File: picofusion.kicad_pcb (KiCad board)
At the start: 2 copper layers, 1 part

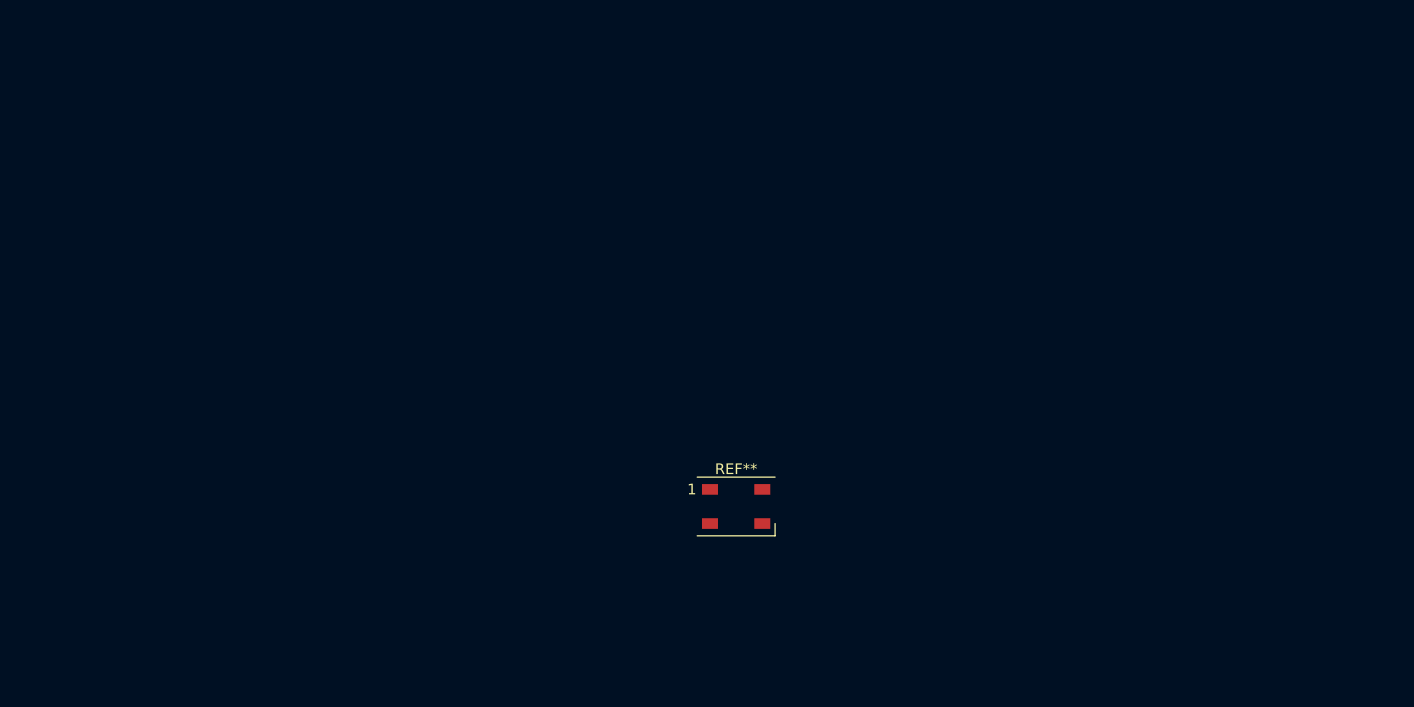
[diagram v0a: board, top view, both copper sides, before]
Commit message: finish schematic draft
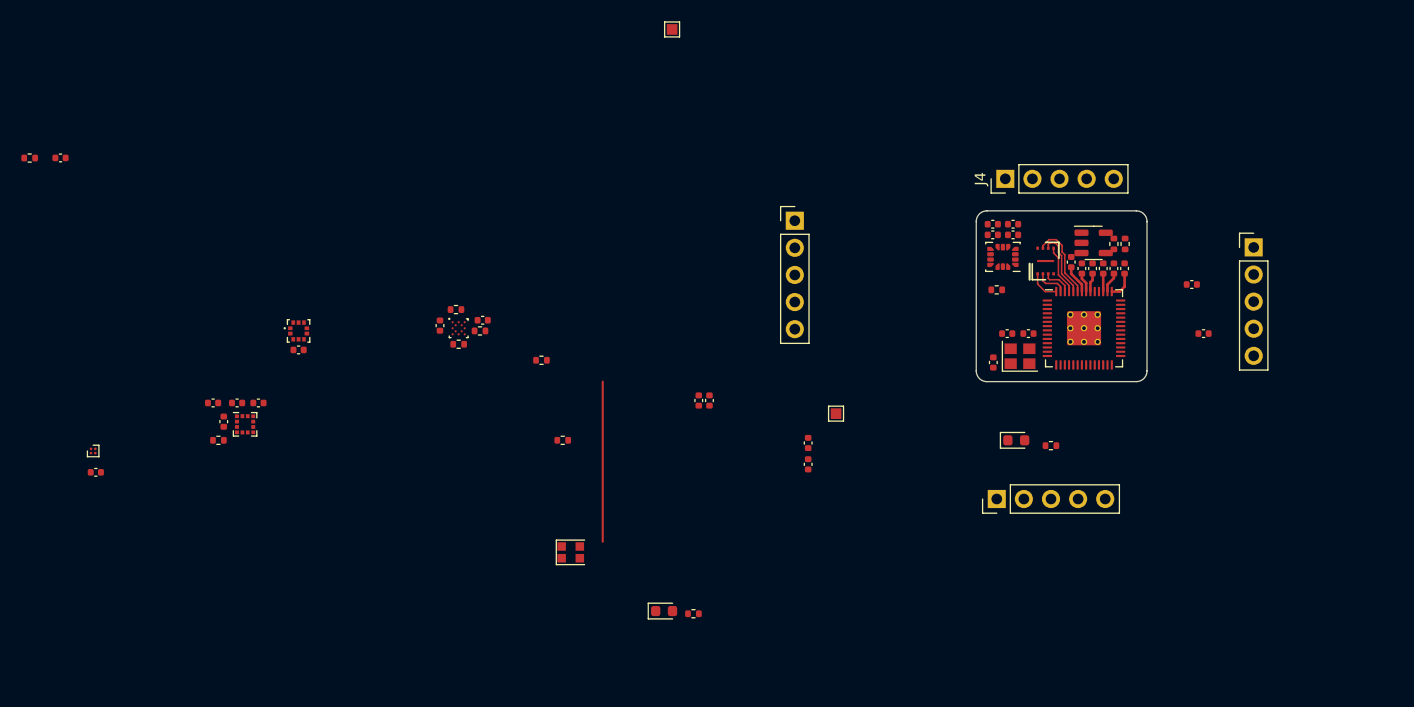
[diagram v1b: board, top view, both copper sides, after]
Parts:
- removed REF**: LED_WS2812B_PLCC4_5.0x5.0mm_P3.2mm, LED_SMD:LED_WS2812B_PLCC4_5.0x5.0mm_P3.2mm
- added C1: 0.1uF, Capacitor_SMD:C_0402_1005Metric, F.Cu at (154.9, 38.8)
- added C10: 0.1uF, Capacitor_SMD:C_0402_1005Metric, F.Cu at (155.9, 39.4)
- added C11: 0.1uF, Capacitor_SMD:C_0402_1005Metric, F.Cu at (60.2, 29.0)
- added C12: 0.1uF, Capacitor_SMD:C_0402_1005Metric, F.Cu at (156.9, 39.4)
- added C13: 0.1uF, Capacitor_SMD:C_0402_1005Metric, F.Cu at (159.9, 39.4)
- added C14: 0.1uF, Capacitor_SMD:C_0402_1005Metric, F.Cu at (166.2, 40.9)
- added C15: 1uF, Capacitor_SMD:C_0402_1005Metric, F.Cu at (158.9, 39.4)
- added C16: 1uF, Capacitor_SMD:C_0402_1005Metric, F.Cu at (130.2, 55.8)
- added C17: 1uF, Capacitor_SMD:C_0402_1005Metric, F.Cu at (130.2, 57.8)
- added C19: 2.2uF, Capacitor_SMD:C_0402_1005Metric, F.Cu at (147.6, 36.2)
- added C2: 0.1uF, Capacitor_SMD:C_0402_1005Metric, F.Cu at (121.0, 51.8)
- added C20: 0.1uF, Capacitor_SMD:C_0402_1005Metric, F.Cu at (147.6, 35.2)
- added C21: 0.1uF, Capacitor_SMD:C_0402_1005Metric, F.Cu at (99.8, 44.2)
- added C22: 0.1uF, Capacitor_SMD:C_0402_1005Metric, F.Cu at (95.8, 44.8)
- added C23: 10nF, Capacitor_SMD:C_0402_1005Metric, F.Cu at (149.4, 36.2)
- added C24: 10uF, Capacitor_SMD:C_0402_1005Metric, F.Cu at (75.5, 53.8)
- added C25: 0.1uF, Capacitor_SMD:C_0402_1005Metric, F.Cu at (74.5, 52.0)
- added C26: 0.1uF, Capacitor_SMD:C_0402_1005Metric, F.Cu at (78.7, 52.0)
- added C27: 220nF, Capacitor_SMD:C_0402_1005Metric, F.Cu at (76.7, 52.0)
- added C28: 0.1uF, Capacitor_SMD:C_0402_1005Metric, F.Cu at (82.5, 47.0)
- added C29: 2.2uF, Capacitor_SMD:C_0402_1005Metric, F.Cu at (63.5, 58.5)
- added C3: 1uF, Capacitor_SMD:C_0402_1005Metric, F.Cu at (157.9, 39.4)
- added C4: 0.1uF, Capacitor_SMD:C_0402_1005Metric, F.Cu at (149.4, 35.2)
- added C5: 12pF, Capacitor_SMD:C_0402_1005Metric, F.Cu at (147.6, 48.2)
- added C6: 0.1uF, Capacitor_SMD:C_0402_1005Metric, F.Cu at (150.9, 45.5)
- added C7: 0.1uF, Capacitor_SMD:C_0402_1005Metric, F.Cu at (167.3, 45.5)
- added C8: 12pF, Capacitor_SMD:C_0402_1005Metric, F.Cu at (148.9, 45.5)
- added C9: 0.1uF, Capacitor_SMD:C_0402_1005Metric, F.Cu at (120.0, 51.8)
- added D1: WS2812B-2020, LED_SMD_Extra:WS2812B-2020, F.Cu at (108.0, 66.0)
- added D2: RED, LED_SMD:LED_0603_1608Metric, F.Cu at (116.8, 71.5)
- added D3: LED, LED_SMD:LED_0603_1608Metric, F.Cu at (149.8, 55.5)
- added J1: EAST, Connector_PinHeader_2.54mm:PinHeader_1x05_P2.54mm_Vertical, F.Cu at (129.0, 34.9)
- added J2: WEST, Connector_PinHeader_2.54mm:PinHeader_1x05_P2.54mm_Vertical, F.Cu at (147.9, 61.0)
- added J3: SOUTH, Connector_PinHeader_2.54mm:PinHeader_1x05_P2.54mm_Vertical, F.Cu at (172.0, 37.4)
- added J4: NORTH, Connector_PinHeader_2.54mm:PinHeader_1x05_P2.54mm_Vertical, F.Cu at (148.7, 31.0)
- added R1: 10K, Resistor_SMD:R_0402_1005Metric, F.Cu at (57.3, 29.1)
- added R13: 10K, Resistor_SMD:R_0402_1005Metric, F.Cu at (147.9, 41.4)
- added R14: 10K, Resistor_SMD:R_0402_1005Metric, F.Cu at (97.2, 43.2)
- added R15: 10K, Resistor_SMD:R_0402_1005Metric, F.Cu at (97.5, 46.5)
- added R16: 10K, Resistor_SMD:R_0402_1005Metric, F.Cu at (99.5, 45.2)
- added R17: 10K, Resistor_SMD:R_0402_1005Metric, F.Cu at (75.0, 55.5)
- added R18: 1K, Resistor_SMD:R_0402_1005Metric, F.Cu at (153.0, 56.0)
- added R2: 27.4, Resistor_SMD:R_0402_1005Metric, F.Cu at (158.9, 37.1)
- added R3: 27.4, Resistor_SMD:R_0402_1005Metric, F.Cu at (159.9, 37.1)
- added R4: 10K, Resistor_SMD:R_0402_1005Metric, F.Cu at (105.3, 48.0)
- added R5: 10K, Resistor_SMD:R_0402_1005Metric, F.Cu at (107.2, 55.5)
- added R6: 1K, Resistor_SMD:R_0402_1005Metric, F.Cu at (119.5, 71.8)
- added TP1: QSPI_SCK, TestPoint:TestPoint_Pad_1.0x1.0mm, F.Cu at (117.5, 17.0)
- added TP2: TestPoint, TestPoint:TestPoint_Pad_1.0x1.0mm, F.Cu at (132.9, 53.0)
- added U1: W25Q16, USON:8-USON, F.Cu at (152.5, 38.7)
- added U2: RP2040, RP2040_minimal:RP2040-QFN-56, F.Cu at (156.1, 45.0)
- added U3: BL9161-33BARN, Package_TO_SOT_SMD:SOT-23-5, F.Cu at (157.0, 37.0)
- added U4: ICM42605, Package_LGA:LGA-14_3x2.5mm_P0.5mm_LayoutBorder3x4y, F.Cu at (148.5, 38.3)
- added U5: BMM150, Package_CSP:WLCSP-12_1.56x1.56mm_P0.4mm, F.Cu at (97.5, 45.0)
- added U6: LIS2MDLTR, Package_LGA:LGA-12_2x2mm_P0.5mm, F.Cu at (77.5, 54.0)
- added U7: ICP-10100, ICP-10100:PQFN50P200X200X80-10N, F.Cu at (82.5, 45.2)
- added U8: MMC5633NJL, Package_BGA:WLP-4_0.86x0.86mm_P0.4mm, F.Cu at (63.2, 56.5)
- added Y1: 12MHz, Crystal:Crystal_SMD_2520-4Pin_2.5x2.0mm, F.Cu at (150.1, 47.6)
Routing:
- net +3V3: track 0.00 -> 8.16 mm
- net /QSPI_SD3: track 0.00 -> 7.41 mm
- net /QSPI_SCLK: track 0.00 -> 6.33 mm
- net /QSPI_SD0: track 0.00 -> 4.66 mm
- net +1V1: track 0.00 -> 4.38 mm
- net /QSPI_SS: track 0.00 -> 3.00 mm
- net /QSPI_SD1: track 0.00 -> 2.99 mm
- net /QSPI_SD2: track 0.00 -> 2.82 mm
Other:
- board outline added: 16 x 16 mm
- copper layers 2 -> 4

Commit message: schematic: update regulator, sensors
* simplify some sensor schematics
* replace 3v3 regulator
* DRC and footprints
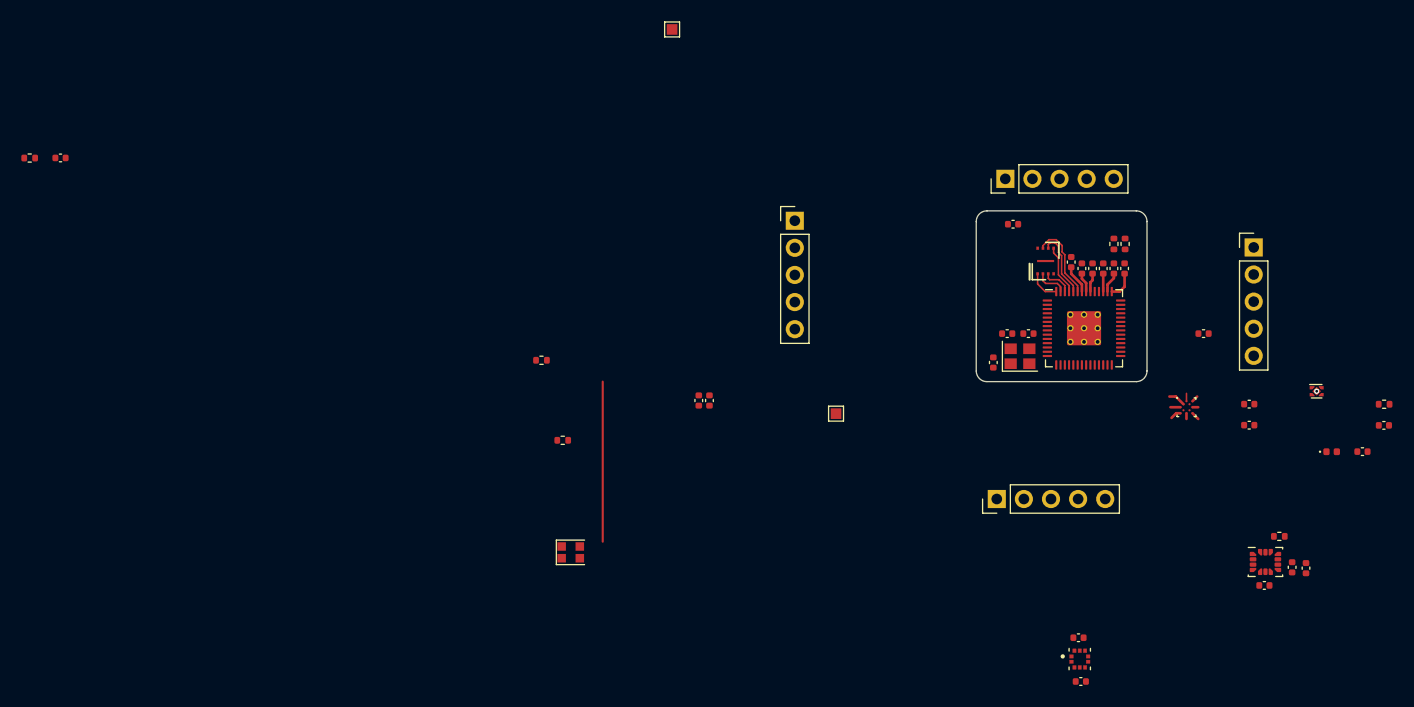
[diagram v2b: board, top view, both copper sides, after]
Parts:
- removed C24: 10uF, Capacitor_SMD:C_0402_1005Metric
- removed C25, C26, C28: 0.1uF, Capacitor_SMD:C_0402_1005Metric
- removed C27: 220nF, Capacitor_SMD:C_0402_1005Metric
- removed C29: 2.2uF, Capacitor_SMD:C_0402_1005Metric
- removed D3: LED, LED_SMD:LED_0603_1608Metric
- removed R13, R14, R15, R16, R17: 10K, Resistor_SMD:R_0402_1005Metric
- removed R18: 1K, Resistor_SMD:R_0402_1005Metric
- removed U7: ICP-10100, ICP-10100:PQFN50P200X200X80-10N
- removed U8: MMC5633NJL, Package_BGA:WLP-4_0.86x0.86mm_P0.4mm
- added C18: 0.1uF, Capacitor_SMD:C_0402_1005Metric, F.Cu at (175.6, 67.4)
- added R7: 10K, Resistor_SMD:R_0402_1005Metric, F.Cu at (174.4, 64.5)
- C16: value 1uF -> 0.1uF
- C17: value 1uF -> 2.2uF
- C19: value 2.2uF -> 10nF
- C23: value 10nF -> 0.1uF
- D2: footprint LED_SMD:LED_0603_1608Metric -> LED_SMD:LED_0402_1005Metric
- R6: value 1K -> 470
- U3: value BL9161-33BARN -> TLV71333PDQNT; footprint Package_TO_SOT_SMD:SOT-23-5 -> Package_SON:Texas_X2SON-4_1x1mm_P0.65mm
- U6: value LIS2MDLTR -> ICP20100; footprint Package_LGA:LGA-12_2x2mm_P0.5mm -> ICP20100:PQFN50P200X200X85-10N
- moved U6 81.2 mm to (155.7, 76.0)
- moved C21 72.5 mm to (171.6, 54.1)
- moved C22 68.7 mm to (155.8, 78.1), turned to 0 degrees
- moved U5 68.6 mm to (165.7, 52.4)
- moved R6 67.6 mm to (184.2, 52.1)
- moved D2 64.3 mm to (179.3, 56.6)
- moved C16 51.9 mm to (182.2, 56.6), turned to 0 degrees
- moved C17 47.7 mm to (176.9, 67.5)
- moved C19 41.6 mm to (173.0, 69.1), turned to 0 degrees
- moved C23 38.2 mm to (155.6, 74.0)
- moved U4 37.7 mm to (173.1, 66.9), turned to 0 degrees
- moved C20 29.4 mm to (171.6, 52.1), turned to 0 degrees
- moved U3 25.1 mm to (177.9, 50.9)
- moved C14 22.3 mm to (184.2, 54.1)
- renumbered TP2 to 3V3
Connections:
- C14 pad 1: +3V3 -> +5V
- C16 pad 1: +5V -> +3V3
- C17 pad 1: +3V3 -> GND
- C17 pad 2: GND -> +3V3
- C19 pad 1: GND -> +3V3
- C19 pad 2: +3V3 -> GND
- C22 pad 1: +3V3 -> GND
- C22 pad 2: GND -> +3V3
- U2 pad 2: /SPI0_MISO -> /SPI0_POCI
- U2 pad 5: /SPI0_MOSI -> /SPI0_POCI
- U2 pad 8: /DRDY_LIS2MDL -> /SPI0_nCS
- U2 pad 9: /DRDY_BMM150 -> unconnected-(U2-Pad9)
- U3 pad 4: (no net) -> unconnected-(U3-Pad4)
- U4 pad 12: Net-(R13-Pad2) -> /SPI0_nCS
- U4 pad 9: unconnected-(U4-Pad9) -> GND
- U5 pad A1: Net-(R16-Pad1) -> +3V3
- U5 pad A5: Net-(R15-Pad1) -> GND
- U5 pad C1: Net-(R14-Pad1) -> GND
- U5 pad D4: /DRDY_BMM150 -> unconnected-(U5-PadD4)
- U6 pad 1: /I2C0_SCL -> +3V3
- U6 pad 2: (no net) -> /I2C0_SCL
- U6 pad 3: Net-(R17-Pad1) -> GND
- U6 pad 5: Net-(C27-Pad1) -> +3V3
- U6 pad 7: /DRDY_LIS2MDL -> unconnected-(U6-Pad7)
- U6 pad 9: +3V3 -> GND
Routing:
- net GND: track 0.00 -> 3.63 mm
- net +3V3: track 8.16 -> 10.5 mm, vias 0 -> 1
- net /I2C0_SCL: track 0.00 -> 0.73 mm

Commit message: draft layout improvements
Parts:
- moved C17 50.1 mm to (139.6, 34.0), turned to -90 degrees
- moved U4 48.0 mm to (137.3, 34.9)
- moved C18 47.8 mm to (139.6, 35.9), turned to 90 degrees
- moved C19 47.4 mm to (138.1, 37.0)
- moved R7 47.1 mm to (136.1, 37.0)
- moved C14 44.3 mm to (142.1, 40.4), turned to -90 degrees
- moved D1 42.7 mm to (148.2, 51.5)
- moved C16 42.4 mm to (143.6, 39.1)
- moved U3 35.9 mm to (143.6, 40.4)
- moved C7 16.8 mm to (150.8, 42.4), turned to 180 degrees
- moved R3 2.15 mm to (157.8, 37.0)
- moved R2 2.10 mm to (156.8, 37.0)
- moved C4 1.95 mm to (149.4, 37.2)
- moved C1 0.40 mm to (154.9, 39.2)
- moved C12 0.40 mm to (156.9, 39.8)
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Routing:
- net /XOUT: track 0.00 -> 2.18 mm
- net /XIN: track 0.00 -> 1.58 mm
- net +1V1: track 4.38 -> 3.58 mm

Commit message: backup before moving to 0201
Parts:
- moved C22 36.2 mm to (141.1, 45.0), turned to -90 degrees
- moved U6 35.3 mm to (139.3, 44.7)
- moved C23 35.2 mm to (139.0, 42.9)
- moved C17 12.0 mm to (150.6, 38.6)
- moved C18 12.0 mm to (150.6, 40.5)
- moved R7 11.9 mm to (147.2, 41.3)
- moved C19 11.9 mm to (149.2, 41.3)
- moved U4 11.9 mm to (148.3, 39.2)
- moved R2 0.49 mm to (156.8, 37.5)
- moved R3 0.49 mm to (157.8, 37.5)
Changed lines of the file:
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@@
   )
   (footprint "Capacitor_SMD:C_0402_1005Metric" (layer "F.Cu")
-    (at 139.6 34 -90)
+    (at 150.6375 38.65 -90)
     (descr "Capacitor SMD 0402 (1005 Metric), square (rectangular) end terminal, IPC_7351 nominal, (Body size source: IPC-SM-782 page 76, https://www.pcb-3d.com/wordpress/wp-content/uploads/ipc-sm-782a_amendment_1_and_2.pdf), generated with kicad-footprint-generator")
     (tags "capacitor")
@@
   )
   (footprint "Package_LGA:LGA-14_3x2.5mm_P0.5mm_LayoutBorder3x4y" (layer "F.Cu")
-    (at 137.3 34.92)
+    (at 148.3375 39.25)
     (descr "LGA, 14 Pin (http://www.st.com/resource/en/datasheet/lsm6ds3.pdf), generated with kicad-footprint-generator ipc_noLead_generator.py")
     (tags "LGA NoLead")
@@
   )
   (footprint "Capacitor_SMD:C_0402_1005Metric" (layer "F.Cu")
-    (at 139.6 35.9 90)
+    (at 150.6375 40.55 90)
     (descr "Capacitor SMD 0402 (1005 Metric), square (rectangular) end terminal, IPC_7351 nominal, (Body size source: IPC-SM-782 page 76, https://www.pcb-3d.com/wordpress/wp-content/uploads/ipc-sm-782a_amendment_1_and_2.pdf), generated with kicad-footprint-generator")
     (tags "capacitor")
@@
   )
   (footprint "Resistor_SMD:R_0402_1005Metric" (layer "F.Cu")
-    (at 156.8 37 90)
+    (at 156.8 37.49 90)
     (descr "Resistor SMD 0402 (1005 Metric), square (rectangular) end terminal, IPC_7351 nominal, (Body size source: IPC-SM-782 page 72, https://www.pcb-3d.com/wordpress/wp-content/uploads/ipc-sm-782a_amendment_1_and_2.pdf), generated with kicad-footprint-generator")
     (tags "resistor")
@@
   )
   (footprint "ICP20100:PQFN50P200X200X85-10N" (layer "F.Cu")
-    (at 155.7 76)
+    (at 139.3 44.7)
     (property "Sheetfile" "sensors.kicad_sch")
     (property "Sheetname" "Sensor Suite")
@@
   )
   (footprint "Resistor_SMD:R_0402_1005Metric" (layer "F.Cu")
-    (at 136.11 37)
+    (at 147.2375 41.33)
     (descr "Resistor SMD 0402 (1005 Metric), square (rectangular) end terminal, IPC_7351 nominal, (Body size source: IPC-SM-782 page 72, https://www.pcb-3d.com/wordpress/wp-content/uploads/ipc-sm-782a_amendment_1_and_2.pdf), generated with kicad-footprint-generator")
     (tags "resistor")
@@
   )
   (footprint "Capacitor_SMD:C_0402_1005Metric" (layer "F.Cu")
-    (at 138.12 37)
+    (at 149.1575 41.33)
     (descr "Capacitor SMD 0402 (1005 Metric), square (rectangular) end terminal, IPC_7351 nominal, (Body size source: IPC-SM-782 page 76, https://www.pcb-3d.com/wordpress/wp-content/uploads/ipc-sm-782a_amendment_1_and_2.pdf), generated with kicad-footprint-generator")
     (tags "capacitor")
@@
   )
   (footprint "Capacitor_SMD:C_0402_1005Metric" (layer "F.Cu")
-    (at 155.8 78.1)
+    (at 141.1 45 -90)
     (descr "Capacitor SMD 0402 (1005 Metric), square (rectangular) end terminal, IPC_7351 nominal, (Body size source: IPC-SM-782 page 76, https://www.pcb-3d.com/wordpress/wp-content/uploads/ipc-sm-782a_amendment_1_and_2.pdf), generated with kicad-footprint-generator")
     (tags "capacitor")
@@
     (property "Sheetname" "Sensor Suite")
     (attr smd)
-    (fp_text reference "C22" (at 0 -1.16) (layer "F.SilkS") hide
-      (effects (font (size 1 1) (thickness 0.15)))
-    )
-    (fp_text value "0.1uF" (at 0 1.16) (layer "F.Fab")
-      (effects (font (size 1 1) (thickness 0.15)))
-    )
-    (fp_text user "${REFERENCE}" (at 0 0) (layer "F.Fab")
-      (effects (font (size 0.25 0.25) (thickness 0.04)))
-    )
-    (fp_line (start -0.107836 -0.36) (end 0.107836 -0.36) (layer "F.SilkS") (width 0.12))
-    (fp_line (start -0.107836 0.36) (end 0.107836 0.36) (layer "F.SilkS") (width 0.12))
-    (fp_line (start 0.91 -0.46) (end 0.91 0.46) (layer "F.CrtYd") (width 0.05))
-    (fp_line (start 0.91 0.46) (end -0.91 0.46) (layer "F.CrtYd") (width 0.05))
-    (fp_line (start -0.91 0.46) (end -0.91 -0.46) (layer "F.CrtYd") (width 0.05))
-    (fp_line (start -0.91 -0.46) (end 0.91 -0.46) (layer "F.CrtYd") (width 0.05))
-    (fp_line (start 0.5 -0.25) (end 0.5 0.25) (layer "F.Fab") (width 0.1))
-    (fp_line (start 0.5 0.25) (end -0.5 0.25) (layer "F.Fab") (width 0.1))
-    (fp_line (start -0.5 -0.25) (end 0.5 -0.25) (layer "F.Fab") (width 0.1))
-    (fp_line (start -0.5 0.25) (end -0.5 -0.25) (layer "F.Fab") (width 0.1))
-    (pad "1" smd roundrect locked (at -0.48 0) (size 0.56 0.62) (layers "F.Cu" "F.Paste" "F.Mask") (roundrect_rratio 0.25)
-      (net 2 "GND") (pintype "passive"))
-    (pad "2" smd roundrect locked (at 0.48 0) (size 0.56 0.62) (layers "F.Cu" "F.Paste" "F.Mask") (roundrect_rratio 0.25)
+    (fp_text reference "C22" (at 0 -1.16 90) (layer "F.SilkS") hide
+      (effects (font (size 1 1) (thickness 0.15)))
+    )
+    (fp_text value "0.1uF" (at 0 1.16 90) (layer "F.Fab")
+      (effects (font (size 1 1) (thickness 0.15)))
+    )
+    (fp_text user "${REFERENCE}" (at 0 0 90) (layer "F.Fab")
+      (effects (font (size 0.25 0.25) (thickness 0.04)))
+    )
+    (fp_line (start -0.107836 -0.36) (end 0.107836 -0.36) (layer "F.SilkS") (width 0.12))
+    (fp_line (start -0.107836 0.36) (end 0.107836 0.36) (layer "F.SilkS") (width 0.12))
+    (fp_line (start 0.91 -0.46) (end 0.91 0.46) (layer "F.CrtYd") (width 0.05))
+    (fp_line (start 0.91 0.46) (end -0.91 0.46) (layer "F.CrtYd") (width 0.05))
+    (fp_line (start -0.91 0.46) (end -0.91 -0.46) (layer "F.CrtYd") (width 0.05))
+    (fp_line (start -0.91 -0.46) (end 0.91 -0.46) (layer "F.CrtYd") (width 0.05))
+    (fp_line (start 0.5 -0.25) (end 0.5 0.25) (layer "F.Fab") (width 0.1))
+    (fp_line (start 0.5 0.25) (end -0.5 0.25) (layer "F.Fab") (width 0.1))
+    (fp_line (start -0.5 -0.25) (end 0.5 -0.25) (layer "F.Fab") (width 0.1))
+    (fp_line (start -0.5 0.25) (end -0.5 -0.25) (layer "F.Fab") (width 0.1))
+    (pad "1" smd roundrect locked (at -0.48 0 270) (size 0.56 0.62) (layers "F.Cu" "F.Paste" "F.Mask") (roundrect_rratio 0.25)
+      (net 2 "GND") (pintype "passive"))
+    (pad "2" smd roundrect locked (at 0.48 0 270) (size 0.56 0.62) (layers "F.Cu" "F.Paste" "F.Mask") (roundrect_rratio 0.25)
       (net 3 "+3V3") (pintype "passive"))
     (model "${KICAD6_3DMODEL_DIR}/Capacitor_SMD.3dshapes/C_0402_1005Metric.wrl"
@@
   )
   (footprint "Capacitor_SMD:C_0402_1005Metric" (layer "F.Cu")
-    (at 155.58 74)
+    (at 139 42.9)
     (descr "Capacitor SMD 0402 (1005 Metric), square (rectangular) end terminal, IPC_7351 nominal, (Body size source: IPC-SM-782 page 76, https://www.pcb-3d.com/wordpress/wp-content/uploads/ipc-sm-782a_amendment_1_and_2.pdf), generated with kicad-footprint-generator")
     (tags "capacitor")
@@
   )
   (footprint "Resistor_SMD:R_0402_1005Metric" (layer "F.Cu")
-    (at 157.8 37 90)
+    (at 157.8 37.49 90)
     (descr "Resistor SMD 0402 (1005 Metric), square (rectangular) end terminal, IPC_7351 nominal, (Body size source: IPC-SM-782 page 72, https://www.pcb-3d.com/wordpress/wp-content/uploads/ipc-sm-782a_amendment_1_and_2.pdf), generated with kicad-footprint-generator")
     (tags "resistor")
@@
     )
   )
-  (gr_line (start 111 50) (end 111 65) (layer "F.Cu") (width 0.2))
   (gr_arc (start 162 49) (mid 161.707107 49.707107) (end 161 50) (layer "Edge.Cuts") (width 0.1))
   (gr_line (start 147 34) (end 161 34) (layer "Edge.Cuts") (width 0.1))
